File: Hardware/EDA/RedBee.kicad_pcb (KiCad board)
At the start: 2 copper layers, 24.4 x 24.5 mm, 3 parts, among them J1 HEADER_F_2.54MM_1R6P_ST_AU_PTH, J2 HEADER_F_2.54MM_1R6P_ST_AU_PTH, P1 XBee Pins Footprint

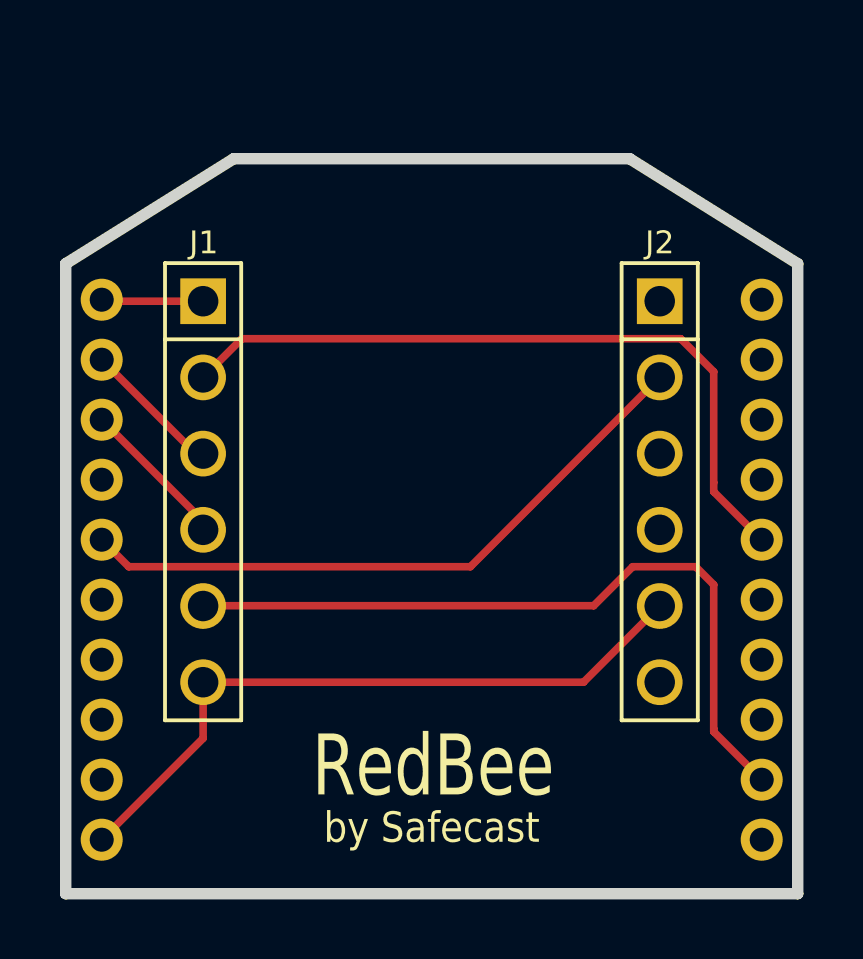
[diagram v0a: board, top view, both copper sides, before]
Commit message: Changed board outline to conform to standard Digi XBee outline. Moved text on silkscreen. Swapped CTS and RTS to correct for DTE perspective. Updated schematic.
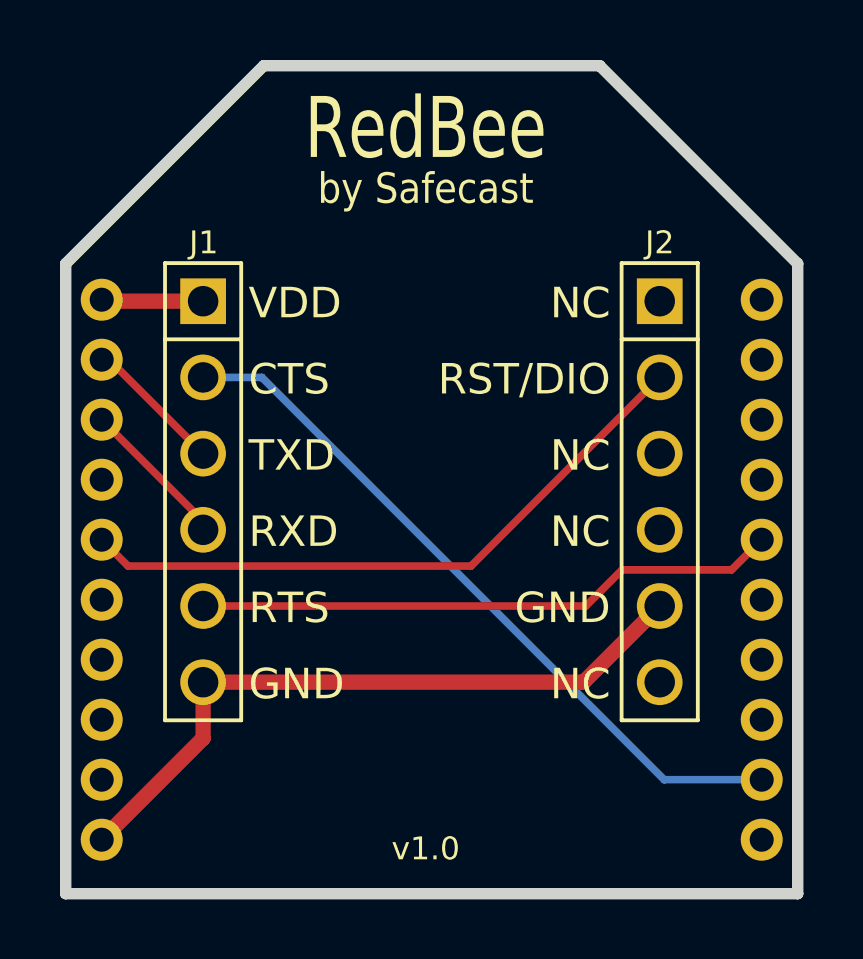
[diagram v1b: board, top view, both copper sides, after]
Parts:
- P1: value XBee Pins Footprint -> HEADER_M_XBEE_PTH
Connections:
- P1 pad 12: RTS_HEADER -> CTS_HEADER
- P1 pad 16: CTS_HEADER -> RTS_HEADER
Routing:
- net RTS_HEADER: track 25.0 -> 19.6 mm
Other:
- board size 24.4 x 24.5 mm -> 24.4 x 27.6 mm
- board text added: "CTS"
- board text added: "GND"
- board text added: "NC"
- board text added: "RST/DIO"
- board text added: "RTS"
- board text added: "RXD"
- board text added: "TXD"
- board text added: "VDD"
- board text added: "v1.0"
- board text removed: "Rev 1.0.0"
